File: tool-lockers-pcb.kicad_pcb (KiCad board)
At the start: 2 copper layers, 80 x 49 mm, 19 parts, among them J1 LOCK, J2 POWER, J3 BUTTON, J4 LED, Q1 Q_NMOS_GSD, SW1 SW_Push, U1 R-78E5.0-1.0, U2 WeMos_D1_mini

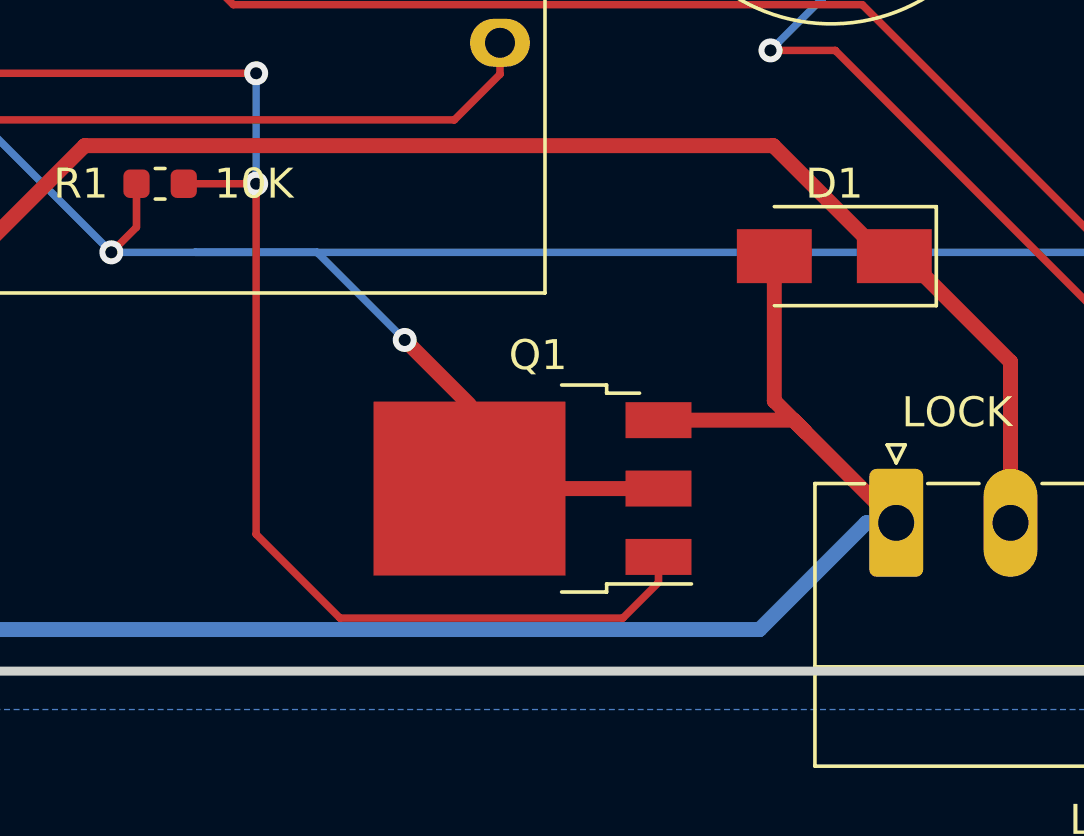
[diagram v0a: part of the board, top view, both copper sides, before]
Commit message: Fix MOSFET footprint and add thermal zone
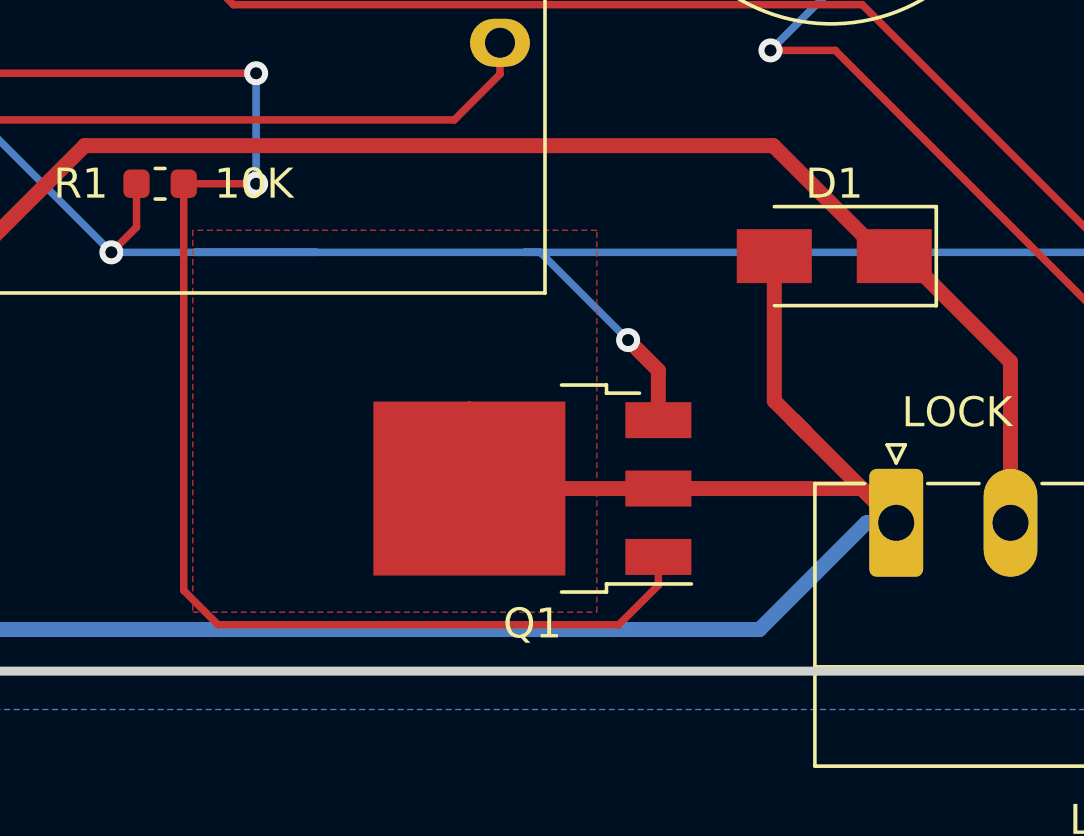
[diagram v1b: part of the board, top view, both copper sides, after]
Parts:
- Q1: value Q_NMOS_GSD -> Q_NMOS_GDS
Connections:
- Q1 pad 2: GND -> /LOCK_RELEASE
- Q1 pad 3: /LOCK_RELEASE -> GND
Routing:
- net /LOCK_RELEASE: track 84.9 -> 97.9 mm
- net GND: track 235.5 -> 226.9 mm
- net /LOCK_RELEASE_SIGNAL: track 50.4 -> 54.1 mm
- added copper zone on F.Cu, net /LOCK_RELEASE
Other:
- board text added: "Designed by Tim Hawes for Edinburgh Hacklab timhawes.com/pcb/locker/2"
- board text removed: "Designed by Tim Hawes for Edinburgh Hacklab github.com/edinburghhacklab/tool-lockers-pcb"
- board text removed: "Rev 1 - 2019-07-11"
